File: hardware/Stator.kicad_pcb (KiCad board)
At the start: 2 copper layers, 200 x 200 mm, 1 part

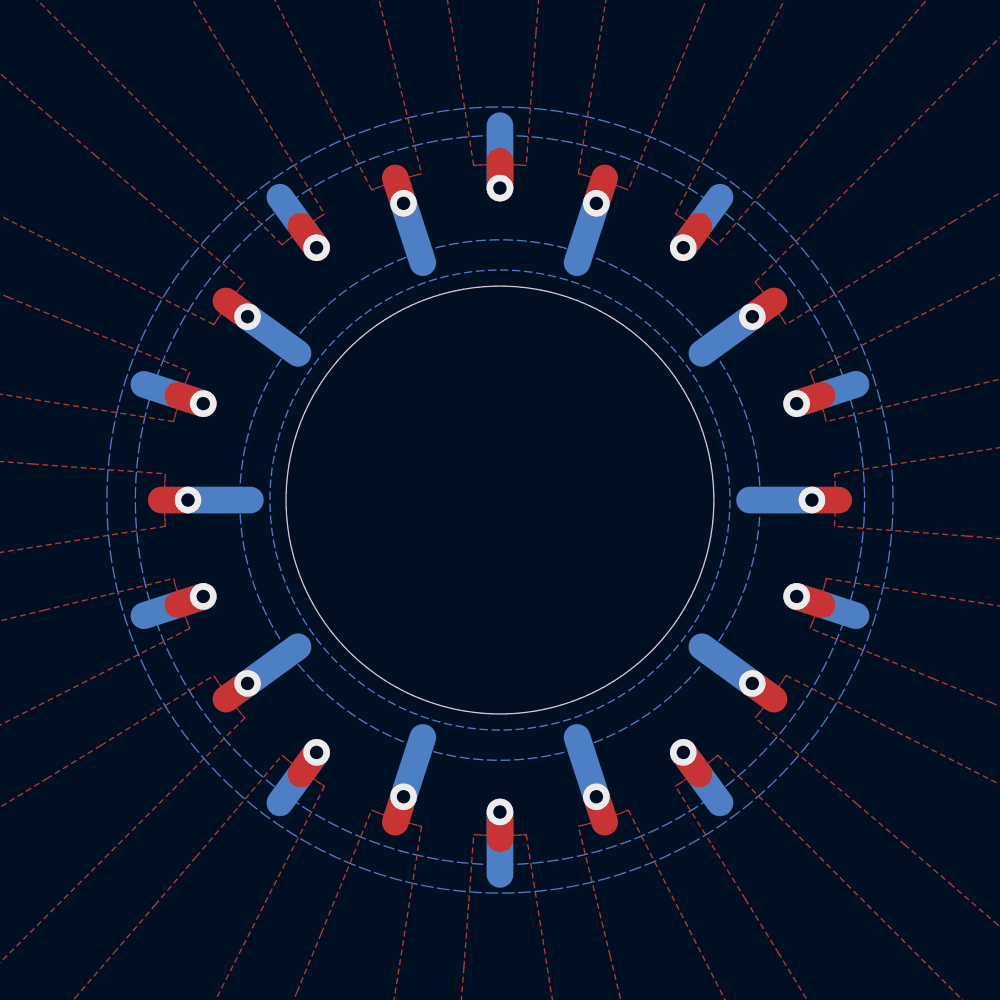
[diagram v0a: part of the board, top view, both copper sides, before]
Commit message: Project update
Updated the project to work with KiCad 10.0.
Updated the exposed pad areas for both layouts.
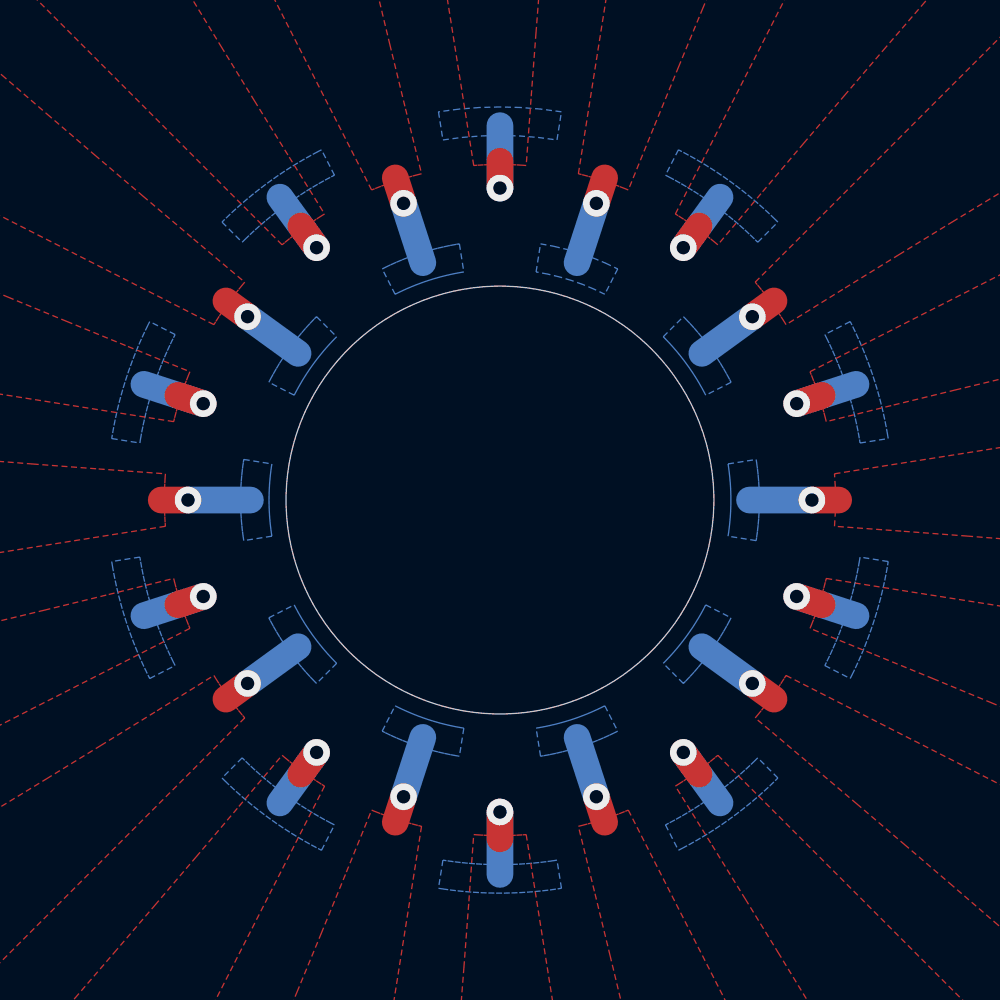
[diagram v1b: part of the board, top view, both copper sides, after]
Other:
- board text added: "PD 22/04/26"
- board text removed: "PD 11/01/26"
